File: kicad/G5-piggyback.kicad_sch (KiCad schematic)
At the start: 5 parts, among them SW1 KSC241GLFS, SW2 RotaryEncoder_Switch_MP, X1 microSD_Card

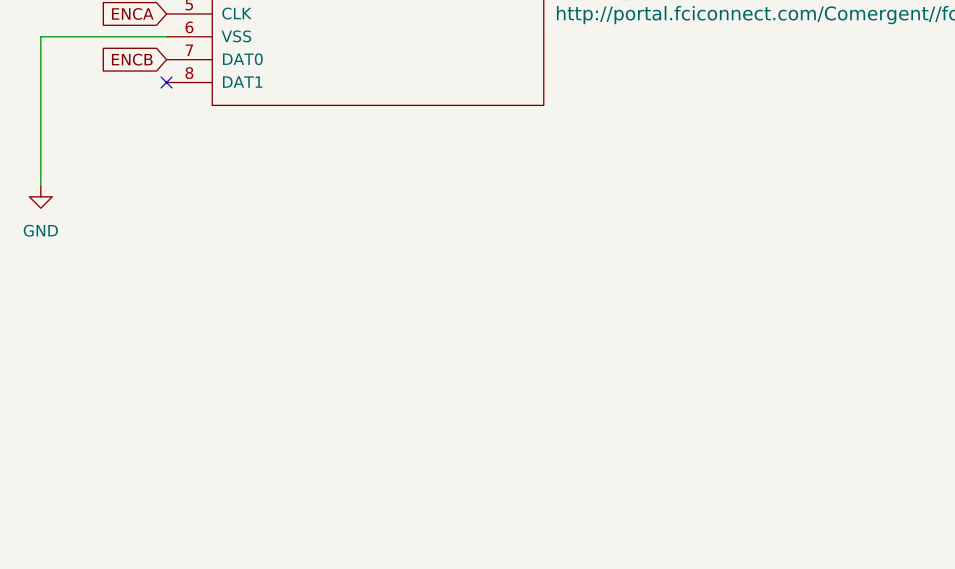
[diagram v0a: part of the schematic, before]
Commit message: Updated layout slightly: centered things vertically, added slightly more space between devboard case and pcb top edge so the microsd click mechanism can hopefully operate without disassembly.
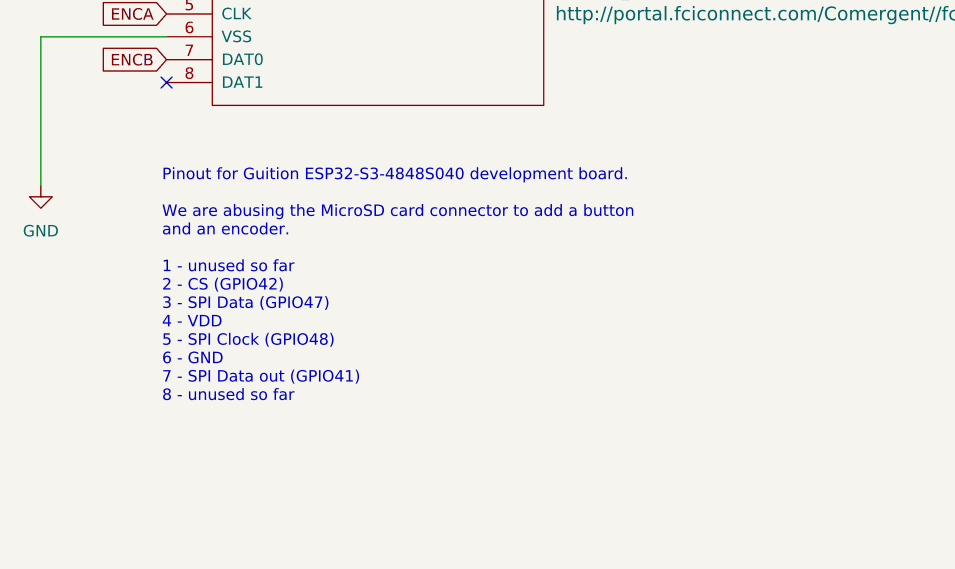
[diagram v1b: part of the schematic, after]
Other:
- note added: "Pinout for Guition ESP32-S3-4848S040 development board. We are abusing the MicroSD card connector to add a button and an encoder. 1 - unused so far 2 - CS (GPIO42) 3 - SPI Data (GPIO47) 4 - VDD 5 - SPI Clock (GPIO48) 6 - GND 7 - SPI Data out (GPIO41) 8 - unused so far"
